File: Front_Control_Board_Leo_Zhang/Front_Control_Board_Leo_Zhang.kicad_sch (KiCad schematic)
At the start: 115 parts, among them J1 22035035, J10 430450200, J11 430450200, J12 430450200, J13 22035035, J14 M22-7130442, J15 M22-7130442, J2 Molex Micro-Fit 4 Pin, J3 430450200, J4 430450200, J5 430450200, J6 430450200, J7 22035035, J8 22035035, J9 22035035, Q1 PSMN5R2-60YL, Q2 PSMN5R2-60YL, Q3 PSMN5R2-60YL, Q4 PSMN5R2-60YL, Q5 PSMN5R2-60YL, Q6 PSMN5R2-60YL, U2 ADS1118IDGS, U3 MCP2562-E-P, U4 MCP6286T-E/OT, U5 UA78M05QDCYRG4Q1, U6 MCP6286T-E/OT, U7 MCP6286T-E/OT

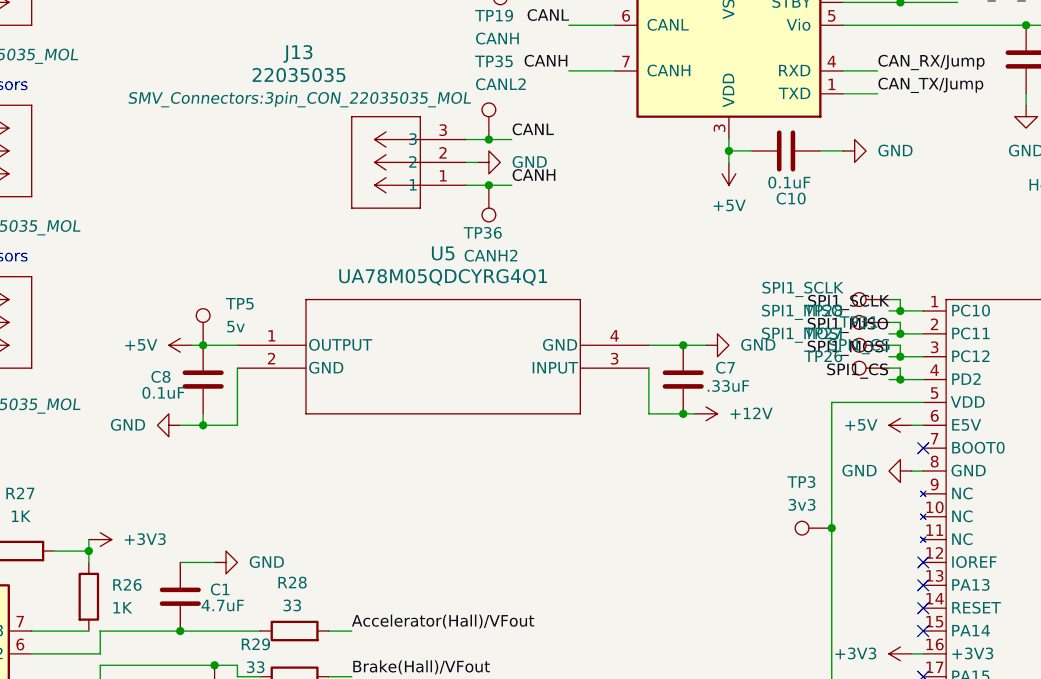
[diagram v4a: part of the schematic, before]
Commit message: LEDs added, mosfet ground polygons, Ground plane, slight rerouting
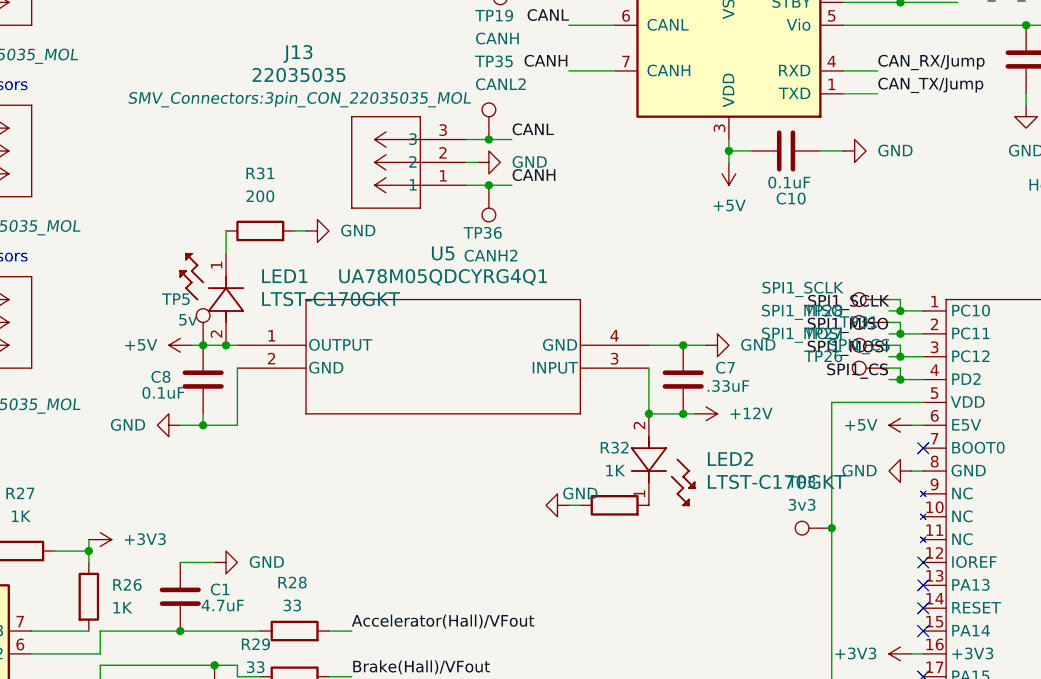
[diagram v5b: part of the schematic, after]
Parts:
- added LED1, LED2: LTST-C170GKT, LED_LTST-C170GKT_LTO, symbol 2026-01-22_04-48-38:LTST-C170GKT
- added R31: 200, Resistor_SMD:R_0805_2012Metric, symbol Device:R
- added R32: 1K, Resistor_SMD:R_0805_2012Metric, symbol Device:R
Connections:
- net +12V: now also LED2.2
- net +5V: now also LED1.2
- net GND: now also R31.2, R32.1
- new net: LED1.1, R31.1
- new net: LED2.1, R32.2

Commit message: made a few layout changes
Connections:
- net CANH renamed CAN_P
- net CANL renamed CAN_N
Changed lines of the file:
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@@
 		)
 	)
-	(label "CANL"
+	(label "CAN_N"
 		(at 113.03 21.59 0)
 		(effects
@@
 		)
 	)
-	(label "CANH"
+	(label "CAN_P"
 		(at 118.11 38.1 180)
 		(effects
@@
 		)
 	)
-	(label "CANL"
+	(label "CAN_N"
 		(at 111.76 45.72 0)
 		(effects
@@
 		)
 	)
-	(label "CANL"
+	(label "CAN_N"
 		(at 118.11 33.02 180)
 		(effects
@@
 		)
 	)
-	(label "CANH"
+	(label "CAN_P"
 		(at 113.03 26.67 0)
 		(effects
@@
 		)
 	)
-	(label "CANH"
+	(label "CAN_P"
 		(at 111.76 50.8 0)
 		(effects
